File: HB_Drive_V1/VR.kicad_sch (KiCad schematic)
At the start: 38 parts, among them J11 Conn_02x02_Odd_Even, J12 Conn_02x04_Counter_Clockwise, J14 Conn_01x02, U15 TL082, U20 TL082, U21 TL082

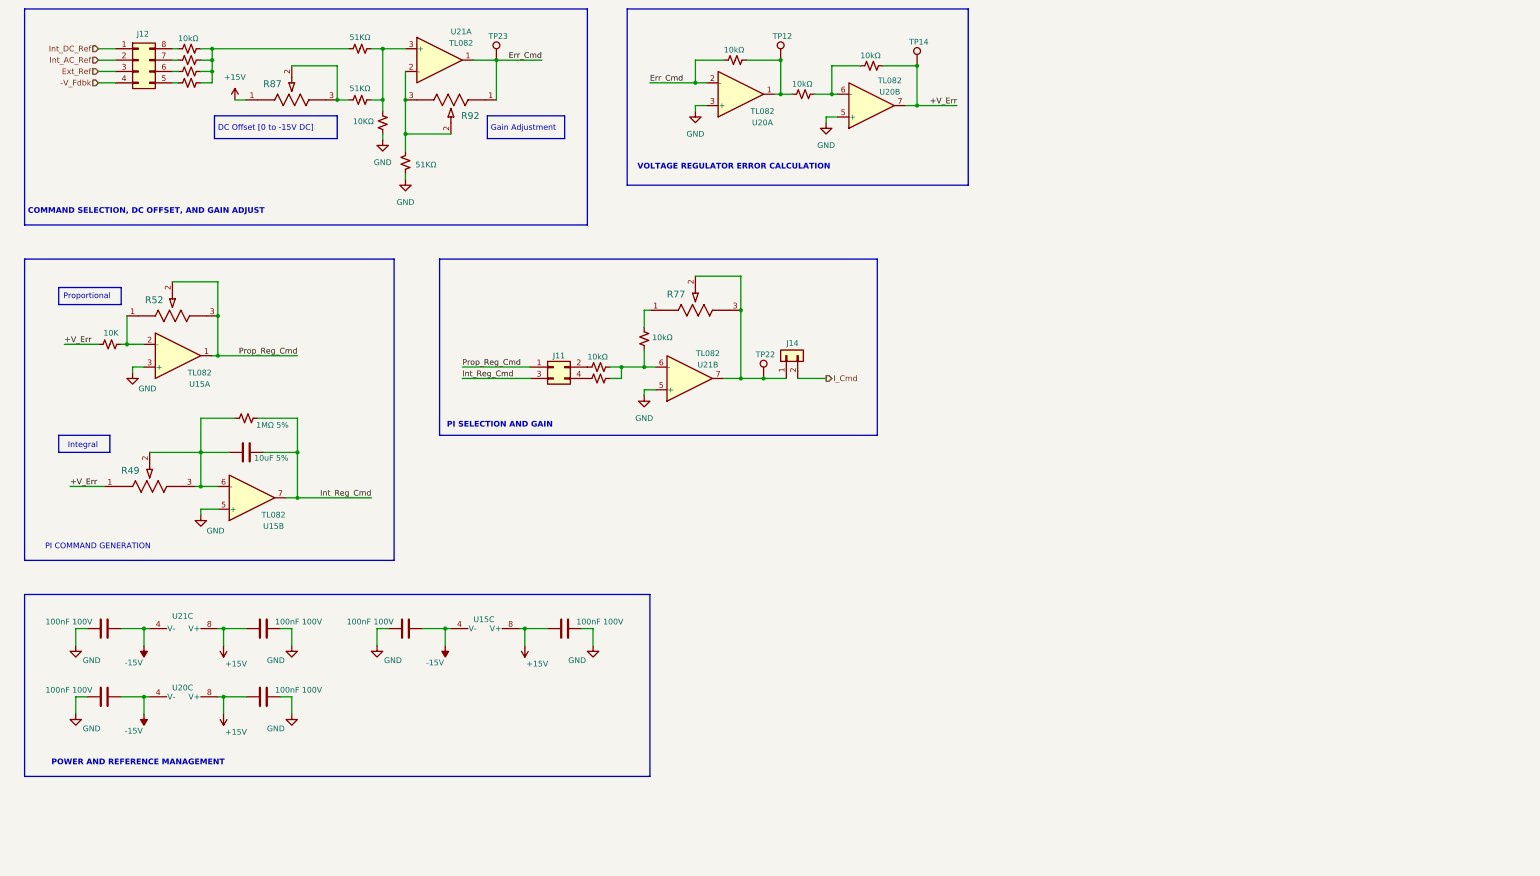
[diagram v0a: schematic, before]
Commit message: finishes hirearchical labels, add 10v +- ref generation and updates the DC offset circuits
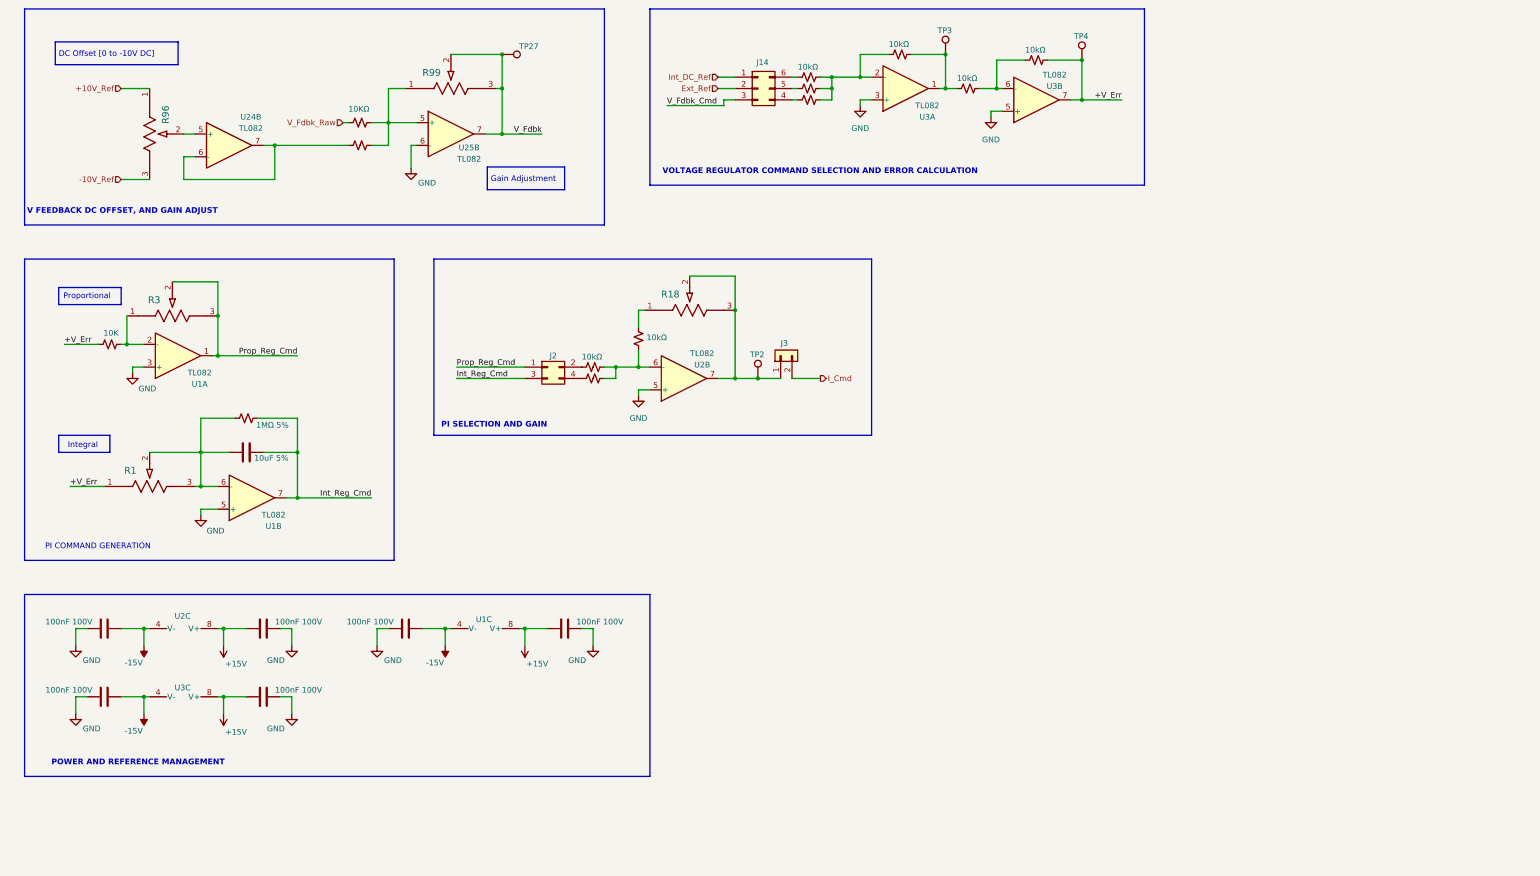
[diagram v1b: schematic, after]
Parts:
- removed J12: Conn_02x04_Counter_Clockwise, Connector_PinSocket_1.27mm:PinSocket_2x04_P1.27mm_Vertical, symbol Connector_Generic:Conn_02x04_Counter_Clockwise
- removed R82: 10kΩ, Resistor_SMD:R_0603_1608Metric_Pad0.98x0.95mm_HandSolder, symbol Device:R_Small_US
- removed R83, R84, R85: 10K, Resistor_SMD:R_0603_1608Metric_Pad0.98x0.95mm_HandSolder, symbol Device:R_Small_US
- removed R87, R92: PV36W104C01B00, PV36W104C01B00:POT_PV36W_BRN, symbol PV36W104C01B00:PV36W104C01B00
- removed R88, R89, R91: 51KΩ, Resistor_SMD:R_0603_1608Metric_Pad0.98x0.95mm_HandSolder, symbol Device:R_Small_US
- removed R90: 10KΩ, Resistor_SMD:R_0603_1608Metric_Pad0.98x0.95mm_HandSolder, symbol Device:R_Small_US
- removed TP23: TestPoint, TestPoint:TestPoint_Loop_D2.60mm_Drill1.6mm_Beaded, symbol Connector:TestPoint
- removed unit 1 of U21
- added J14: Conn_02x03_Counter_Clockwise, Connector_PinSocket_1.27mm:PinSocket_2x03_P1.27mm_Vertical, symbol Connector_Generic:Conn_02x03_Counter_Clockwise
- added R4: 10kΩ, Resistor_SMD:R_0603_1608Metric_Pad0.98x0.95mm_HandSolder, symbol Device:R_Small_US
- added R5, R6: 10K, Resistor_SMD:R_0603_1608Metric_Pad0.98x0.95mm_HandSolder, symbol Device:R_Small_US
- added R96: PV36W104C01B00, PV36W104C01B00:POT_PV36W_BRN, symbol PV36W104C01B00:PV36W104C01B00
- added R97, R98: 10KΩ, Resistor_SMD:R_0603_1608Metric_Pad0.98x0.95mm_HandSolder, symbol Device:R_Small_US
- added R99: PV36W204C01B00, PV36W104C01B00:POT_PV36W_BRN, symbol PV36W104C01B00:PV36W104C01B00
- added TP27: TestPoint, TestPoint:TestPoint_Loop_D2.60mm_Drill1.6mm_Beaded, symbol Connector:TestPoint
- added U24: TL082, Package_SO:SOIC-8_5.3x5.3mm_P1.27mm, symbol Amplifier_Operational:TL082
- added U25: TL082, symbol Amplifier_Operational:TL082
- renumbered C43 to C1, C44 to C2, C27 to C3, C47 to C4, C48 to C5, C45 to C6, C49 to C7, J11 to J2, J14 to J3, R49 to R1, R28 to R15, R29 to R16, R76 to R17, R77 to R18, R59 to R19, R50 to R2, R68 to R20, R69 to R21, R52 to R3, R58 to R9, TP22 to TP2, TP12 to TP3, TP14 to TP4, U15 to U1, U21 to U2, U20 to U3
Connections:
- net Ext_Ref: now also J14.2 (Pin_2)
- net GND: now also U25.6 (-)
- net Int_DC_Ref: now also J14.1 (Pin_1)
- net Err_Cmd: no longer names the net of R19.2, U3.2 (-)
- net Err_Cmd: now also R4.1, R5.2, R6.2
- new net: J14.4 (Pin_4), R6.1
- new net: J14.5 (Pin_5), R5.1
- new net: J14.6 (Pin_6), R4.2
- new net: R97.1, R98.1, R99.1, U25.5 (+)
- new net: R98.2, U24.6 (-), U24.7
- new net: R96.2, U24.5 (+)
- new net +10V_Ref: R96.1
- new net -10V_Ref: R96.3
- new net V_Fdbk: R99.2, R99.3, TP27.1, U25.7
- new net V_Fdbk_Cmd: J14.3 (Pin_3)
- new net V_Fdbk_Raw: R97.2
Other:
- note added: "DC Offset [0 to -10V DC]"
- note added: "V FEEDBACK DC OFFSET, AND GAIN ADJUST"
- note added: "VOLTAGE REGULATOR COMMAND SELECTION AND ERROR CALCULATION"
- note removed: "COMMAND SELECTION, DC OFFSET, AND GAIN ADJUST"
- note removed: "DC Offset [0 to -15V DC]"
- note removed: "VOLTAGE REGULATOR ERROR CALCULATION"
- moved on the sheet: J2, J3, R18, TP2, TP3, TP4, U2B, U3A, U3B

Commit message: updates board to highest working copy
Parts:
- removed J14: Conn_02x03_Counter_Clockwise, Connector_PinSocket_1.27mm:PinSocket_2x03_P1.27mm_Vertical, symbol Connector_Generic:Conn_02x03_Counter_Clockwise
- removed U25: TL082, symbol Amplifier_Operational:TL082
- added C208, C209: 100nF 100V, Capacitor_SMD:C_0603_1608Metric, symbol Device:C
- added J202: Conn_02x03_Odd_Even, Connector_PinHeader_2.54mm:PinHeader_2x03_P2.54mm_Vertical, symbol Connector_Generic:Conn_02x03_Odd_Even
- added R219, R220: 10kΩ, Resistor_SMD:R_0603_1608Metric_Pad0.98x0.95mm_HandSolder, symbol Device:R_Small_US
- added TP205: TestPoint, TestPoint:TestPoint_Loop_D2.60mm_Drill1.6mm_Beaded, symbol Connector:TestPoint
- added unit 2 of U201
- added unit 3 of U204
- added unit 1 of U204
- J201: renamed from J2; footprint Connector_PinSocket_1.27mm:PinSocket_2x02_P1.27mm_Vertical -> Connector_PinHeader_2.54mm:PinHeader_2x02_P2.54mm_Vertical
- U201, U204: renamed from U2; footprint Package_SO:SOIC-8_5.3x5.3mm_P1.27mm -> Package_SO:SOIC-8_3.9x4.9mm_P1.27mm
- U201: renamed from U24; footprint Package_SO:SOIC-8_5.3x5.3mm_P1.27mm -> Package_SO:SOIC-8_3.9x4.9mm_P1.27mm
- U202: renamed from U3; footprint (none) -> Package_SO:SOIC-8_3.9x4.9mm_P1.27mm
- U203: renamed from U1; footprint (none) -> Package_SO:SOIC-8_3.9x4.9mm_P1.27mm
- renumbered C1 to C201, C2 to C202, C3 to C203, C4 to C204, C5 to C205, C6 to C206, C7 to C207, J3 to J203, R1 to R201, R2 to R202, R3 to R203, R96 to R204, R9 to R205, R97 to R206, R98 to R207, R99 to R208, R15 to R209, R16 to R210, R17 to R211, R18 to R212, R4 to R213, R5 to R214, R6 to R215, R19 to R216, R20 to R217, R21 to R218, TP27 to TP201, TP2 to TP202, TP3 to TP203, TP4 to TP204
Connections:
- net +15V: now also C209.2, U204.8 (V+)
- net -15V: now also C208.1, U204.4 (V-)
- net GND: now also C208.2, C209.1, U201.5 (+), U204.3 (+)
- net at R215.1: now also J202.6 (Pin_6)
- net at R214.1: now also J202.4 (Pin_4)
- net at R213.2: now also J202.2 (Pin_2)
- net at R206.1, R207.1, R208.1: now also U201.6 (-)
- net at R204.2: now also U201.3 (+); no longer U201.5 (+)
- net Int_Reg_Cmd renamed -Int_Reg_Cmd
- net Prop_Reg_Cmd renamed -Prop_Reg_Cmd
- net V_Fdbk renamed -V_Fdbk
- net -V_Fdbk: now also J202.5 (Pin_5), R219.2, U201.7
- new net: R219.1, R220.2, U204.2 (-)
- new net: R220.1, TP205.1, U204.1
- new net: R207.2, U201.1, U201.2 (-)
- new net Ext_Cmd: J202.3 (Pin_3)
- new net Int_Cmd: J202.1 (Pin_1)
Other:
- note added: "+V_Fdbk"
- moved on the sheet: J201, J203, R201, R203, R204, R208, R212, TP201, TP202, TP203, TP204, U201A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

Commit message: updates board to REV 1 Ordered version
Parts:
- C203: value 10uF 5% -> 10uF 10%
- R202, R210, R214, R215: value 10K -> 10kΩ 1%
- R206, R207: value 10KΩ -> 10kΩ 1%
- R209, R211, R213, R216, R217, R218, R219, R220: value 10kΩ -> 10kΩ 1%
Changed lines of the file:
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@@
 			)
 		)
-		(property "Value" "10KΩ"
+		(property "Value" "10kΩ 1%"
 			(at 152.146 82.042 90)
 			(show_name no)
@@
 			)
 		)
-		(property "Value" "10uF 5%"
+		(property "Value" "10uF 10%"
 			(at 301.498 104.14 90)
 			(show_name no)
@@
 			)
 		)
-		(property "Value" "10kΩ"
+		(property "Value" "10kΩ 1%"
 			(at 199.136 85.344 90)
 			(show_name no)
@@
 			)
 		)
-		(property "Value" "10K"
+		(property "Value" "10kΩ 1%"
 			(at 112.014 130.81 90)
 			(hide yes)
@@
 			)
 		)
-		(property "Value" "10kΩ"
+		(property "Value" "10kΩ 1%"
 			(at 131.826 120.904 90)
 			(show_name no)
@@
 			)
 		)
-		(property "Value" "10K"
+		(property "Value" "10kΩ 1%"
 			(at 112.014 128.27 90)
 			(hide yes)
@@
 			)
 		)
-		(property "Value" "10kΩ"
+		(property "Value" "10kΩ 1%"
 			(at 162.306 122.174 90)
 			(show_name no)
@@
 			)
 		)
-		(property "Value" "10K"
+		(property "Value" "10kΩ 1%"
 			(at 266.954 158.75 90)
 			(hide yes)
@@
 			)
 		)
-		(property "Value" "10KΩ"
+		(property "Value" "10kΩ 1%"
 			(at 152.146 87.122 90)
 			(hide yes)
@@
 			)
 		)
-		(property "Value" "10kΩ"
+		(property "Value" "10kΩ 1%"
 			(at 111.506 125.984 90)
 			(show_name no)
@@
 			)
 		)
-		(property "Value" "10kΩ"
+		(property "Value" "10kΩ 1%"
 			(at 147.066 128.524 90)
 			(show_name no)
@@
 			)
 		)
-		(property "Value" "10kΩ"
+		(property "Value" "10kΩ 1%"
 			(at 215.646 77.724 90)
 			(show_name no)
@@
 			)
 		)
-		(property "Value" "10kΩ"
+		(property "Value" "10kΩ 1%"
 			(at 266.446 156.464 90)
 			(show_name no)
@@
 			)
 		)
-		(property "Value" "10K"
+		(property "Value" "10kΩ 1%"
 			(at 265.684 76.2 90)
 			(show_name no)
@@
 			)
 		)
-		(property "Value" "10kΩ"
+		(property "Value" "10kΩ 1%"
 			(at 280.924 152.146 0)
 			(show_name no)

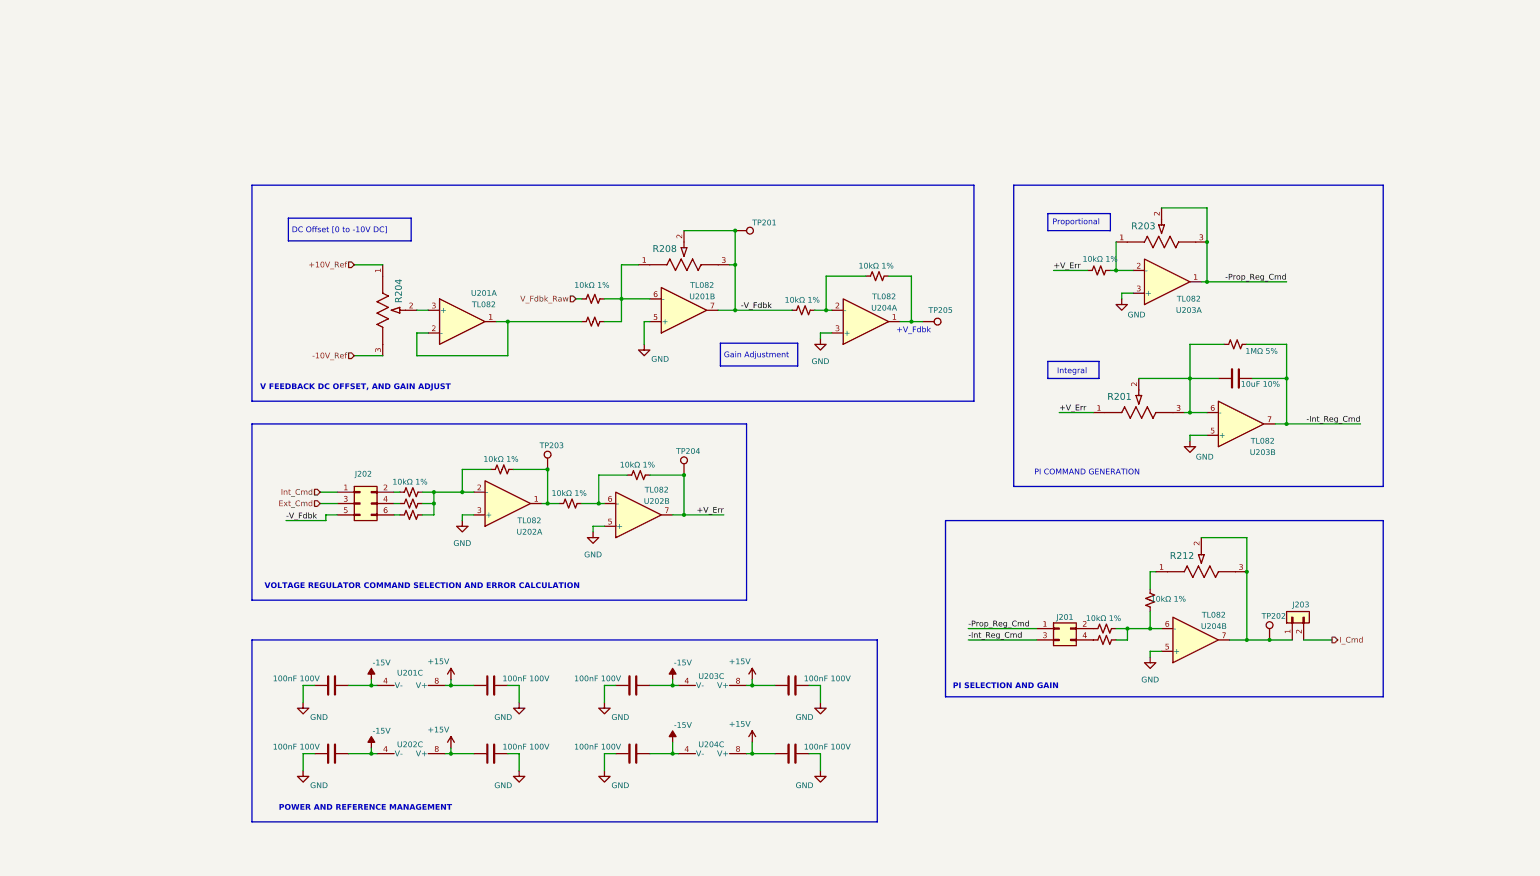
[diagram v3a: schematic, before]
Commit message: Annotates Schematic! Fixes REV1 wiring swaps and replaces buffer
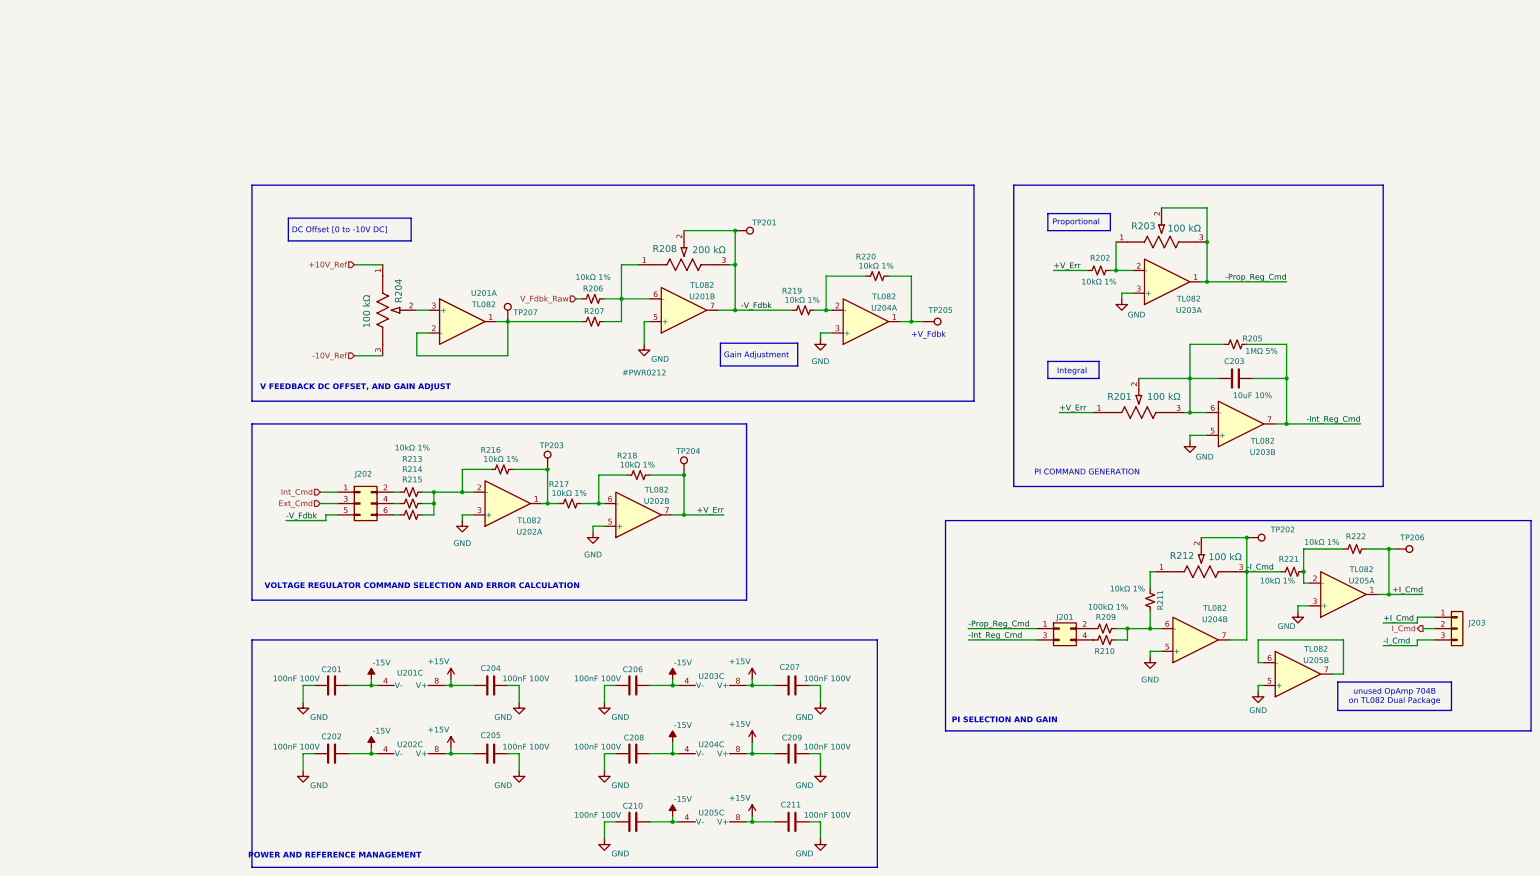
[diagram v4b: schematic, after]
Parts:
- removed J203: Conn_01x02, Connector_PinHeader_1.27mm:PinHeader_1x02_P1.27mm_Vertical, symbol Connector_Generic:Conn_01x02
- added C210, C211: 100nF 100V, Capacitor_SMD:C_0603_1608Metric, symbol Device:C
- added J203: Conn_01x03, symbol Connector_Generic:Conn_01x03
- added R221, R222: 10kΩ 1%, Resistor_SMD:R_0603_1608Metric_Pad0.98x0.95mm_HandSolder, symbol Device:R_Small_US
- added TP206, TP207: TestPoint, TestPoint:TestPoint_Loop_D2.60mm_Drill1.6mm_Beaded, symbol Connector:TestPoint
- added U205: TL082, Package_SO:SOIC-8_3.9x4.9mm_P1.27mm, symbol Amplifier_Operational:TL082
- R201, R203, R204, R212: value PV36W104C01B00 -> 100 kΩ
- R208: value PV36W204C01B00 -> 200 kΩ
- R209: value 10kΩ 1% -> 100kΩ 1%
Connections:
- net +15V: now also C211.2, U205.8 (V+)
- net -15V: now also C210.1, U205.4 (V-)
- net GND: now also C210.2, C211.1, U205.3 (+), U205.5 (+)
- net I_Cmd: now also J203.2 (Pin_2)
- net -I_Cmd: now reaches R212.2, R212.3, TP202.1, U204.7
- net -I_Cmd: now also J203.3 (Pin_3), R221.2
- net at R207.2, U201.1, U201.2 (-): now also TP207.1
- new net: R221.1, R222.2, U205.2 (-)
- new net: U205.6 (-), U205.7
- new net +I_Cmd: J203.1 (Pin_1), R222.1, TP206.1, U205.1
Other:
- note added: "unused OpAmp 704B on TL082 Dual Package"

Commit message: annotates PCB! wiring is still broken here
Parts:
- J203: footprint (none) -> Connector_PinHeader_2.54mm:PinHeader_1x03_P2.54mm_Vertical
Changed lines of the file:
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@@
 			)
 		)
-		(property "Footprint" ""
+		(property "Footprint" "Connector_PinHeader_2.54mm:PinHeader_1x03_P2.54mm_Vertical"
 			(at 345.44 158.75 0)
 			(hide yes)

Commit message: restores v2 to condtion as ordered!
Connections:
- net +I_Cmd: now also J203.3 (Pin_3), R212.2, R212.3, R221.2, TP202.1, U204.7; no longer J203.1 (Pin_1), R222.1, TP206.1, U205.1
- net -I_Cmd: now also J203.1 (Pin_1), R222.1, TP206.1, U205.1; no longer J203.3 (Pin_3), R212.2, R212.3, R221.2, TP202.1, U204.7
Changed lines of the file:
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@@
+		)
+	)
+	(label "+I_Cmd"
+		(at 306.07 146.05 180)
+		(effects
+			(font
+				(size 1.27 1.27)
+			)
+			(justify right bottom)
 		)
 	)
 	(label "-I_Cmd"
-		(at 298.45 146.05 0)
+		(at 328.93 157.48 0)
 		(effects
 			(font
@@
 		)
 	)
-	(label "+I_Cmd"
-		(at 328.93 157.48 0)
-		(effects
-			(font
-				(size 1.27 1.27)
-			)
-			(justify left bottom)
-		)
-	)
 	(label "-V_Fdbk"
 		(at 185.42 87.63 0)
@@
 		)
 	)
-	(label "-Int_Reg_Cmd"
-		(at 236.22 161.29 0)
-		(effects
-			(font
-				(size 1.27 1.27)
-			)
-			(justify left bottom)
-		)
-	)
-	(label "+I_Cmd"
+	(label "-I_Cmd"
 		(at 337.82 151.13 180)
 		(effects
@@
 		)
 	)
-	(label "-I_Cmd"
-		(at 328.93 162.56 0)
+	(label "-Int_Reg_Cmd"
+		(at 236.22 161.29 0)
 		(effects
 			(font
@@
 		(effects
 			(font
+				(size 1.27 1.27)
+			)
+			(justify left bottom)
+		)
+	)
+	(label "+I_Cmd"
+		(at 328.93 162.56 0)
+		(effects
+			(font
